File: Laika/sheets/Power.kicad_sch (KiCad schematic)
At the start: 0 parts

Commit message: Created 3.3V Buck Regulator Circuit
Created schematic for a 3.3V buck regulator. All component selection and
calaculation was performed using TI WEBENCH Power designer, of which the
artifacts are stored in 'calc'. Created Netclasses for PWR and USB.
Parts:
- added C1, C5: 10u, Capacitor_SMD:C_0805_2012Metric, symbol Device:C
- added C2, C3: 100n, Capacitor_SMD:C_0805_2012Metric, symbol Device:C
- added C4, C6: 22u, Capacitor_SMD:C_0805_2012Metric, symbol Device:C
- added L1: 4.7u, Inductor_SMD:L_Bourns-SRN8040_8x8.15mm, symbol Device:L
- added R3: 30, Resistor_SMD:R_0603_1608Metric, symbol Device:R
- added R4: 30.9k, Resistor_SMD:R_0603_1608Metric, symbol Device:R
- added R5: 10k, Resistor_SMD:R_0603_1608Metric, symbol Device:R
- added U3: TPS56339DDC, Package_TO_SOT_SMD:SOT-23-6, symbol Regulator_Switching:TPS56339DDC
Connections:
- new net: C3.1, R3.2
- new net: R4.1, R5.2, U3.4 (FB)
- new net: R3.1, U3.6 (BOOT)
- new net: C4.2, C6.1
- new net: C1.2, C5.1
- new net +3V3: C4.1, L1.2, R4.2
- new net BUCK_OUT: C3.2, L1.1, U3.2 (SW)
- new net GND: C2.2, C5.2, C6.2, R5.1, U3.1 (GND)
- new net VDD: C1.1, C2.1, U3.3 (VIN)
- no-connect marks 0 -> 1
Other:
- note added: "3.3V Buck Regulator"
- note added: "Cbst 100.0 nF 35.47 Ohm"
- note added: "Cin 10.0 uF 5.463 mOhm"
- note added: "Cinx 100.0 nF 35.47 mOhm"
- note added: "Cout 22.0 uF 1.603 mOhm"
- note added: "L1 4.7 uH 24.0 mOhm"
- note added: "Power & Battery Management"
- note added: "Rbst 30.0 Ohm 100.0 mW"
- note added: "Rfbb 10.0 kOhm 100.0 mW"
- note added: "Rfbt 30.9 kOhm 100.0 mW"
- note added: "VinMin = 5.0 V VinMax = 12.0 V Vout = 3.3 V Iout = 2.0 A"

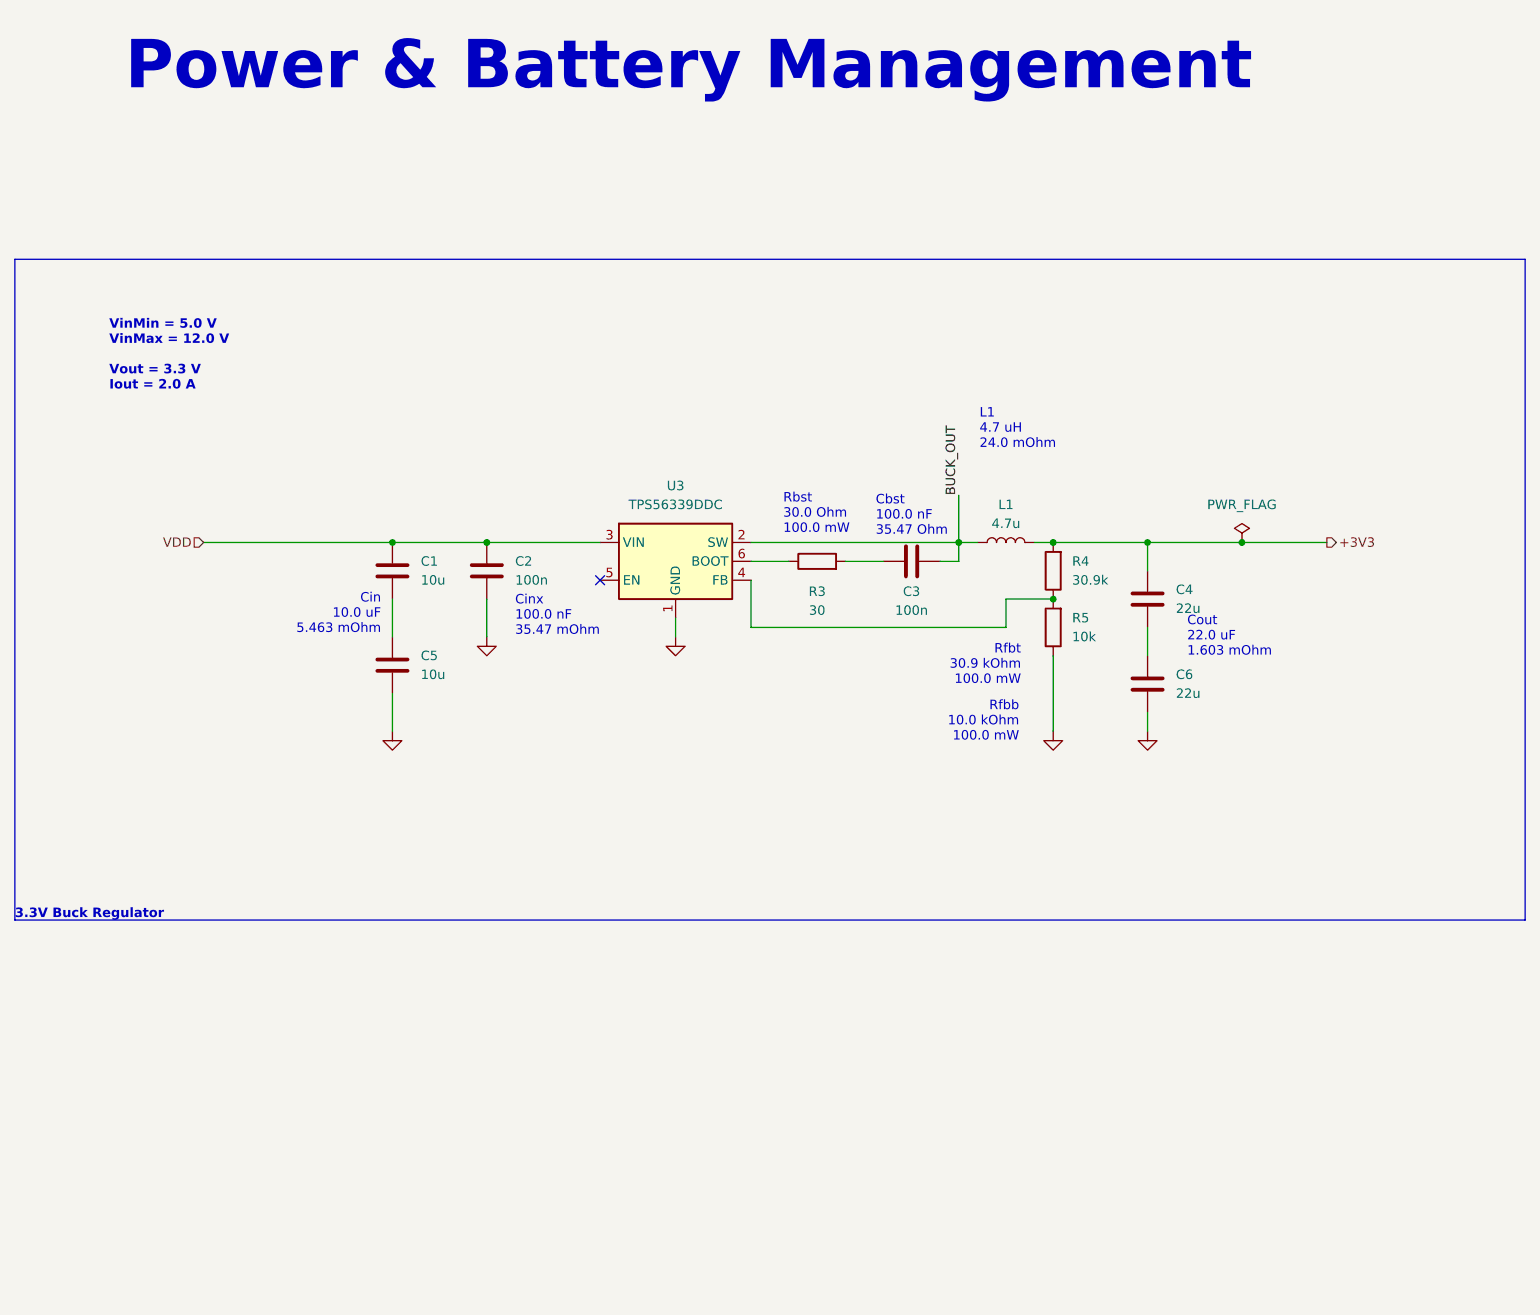
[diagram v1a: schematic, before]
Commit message: Created 1.8V LDO circuit, assigned Mfr Part Numbers to Power IC's
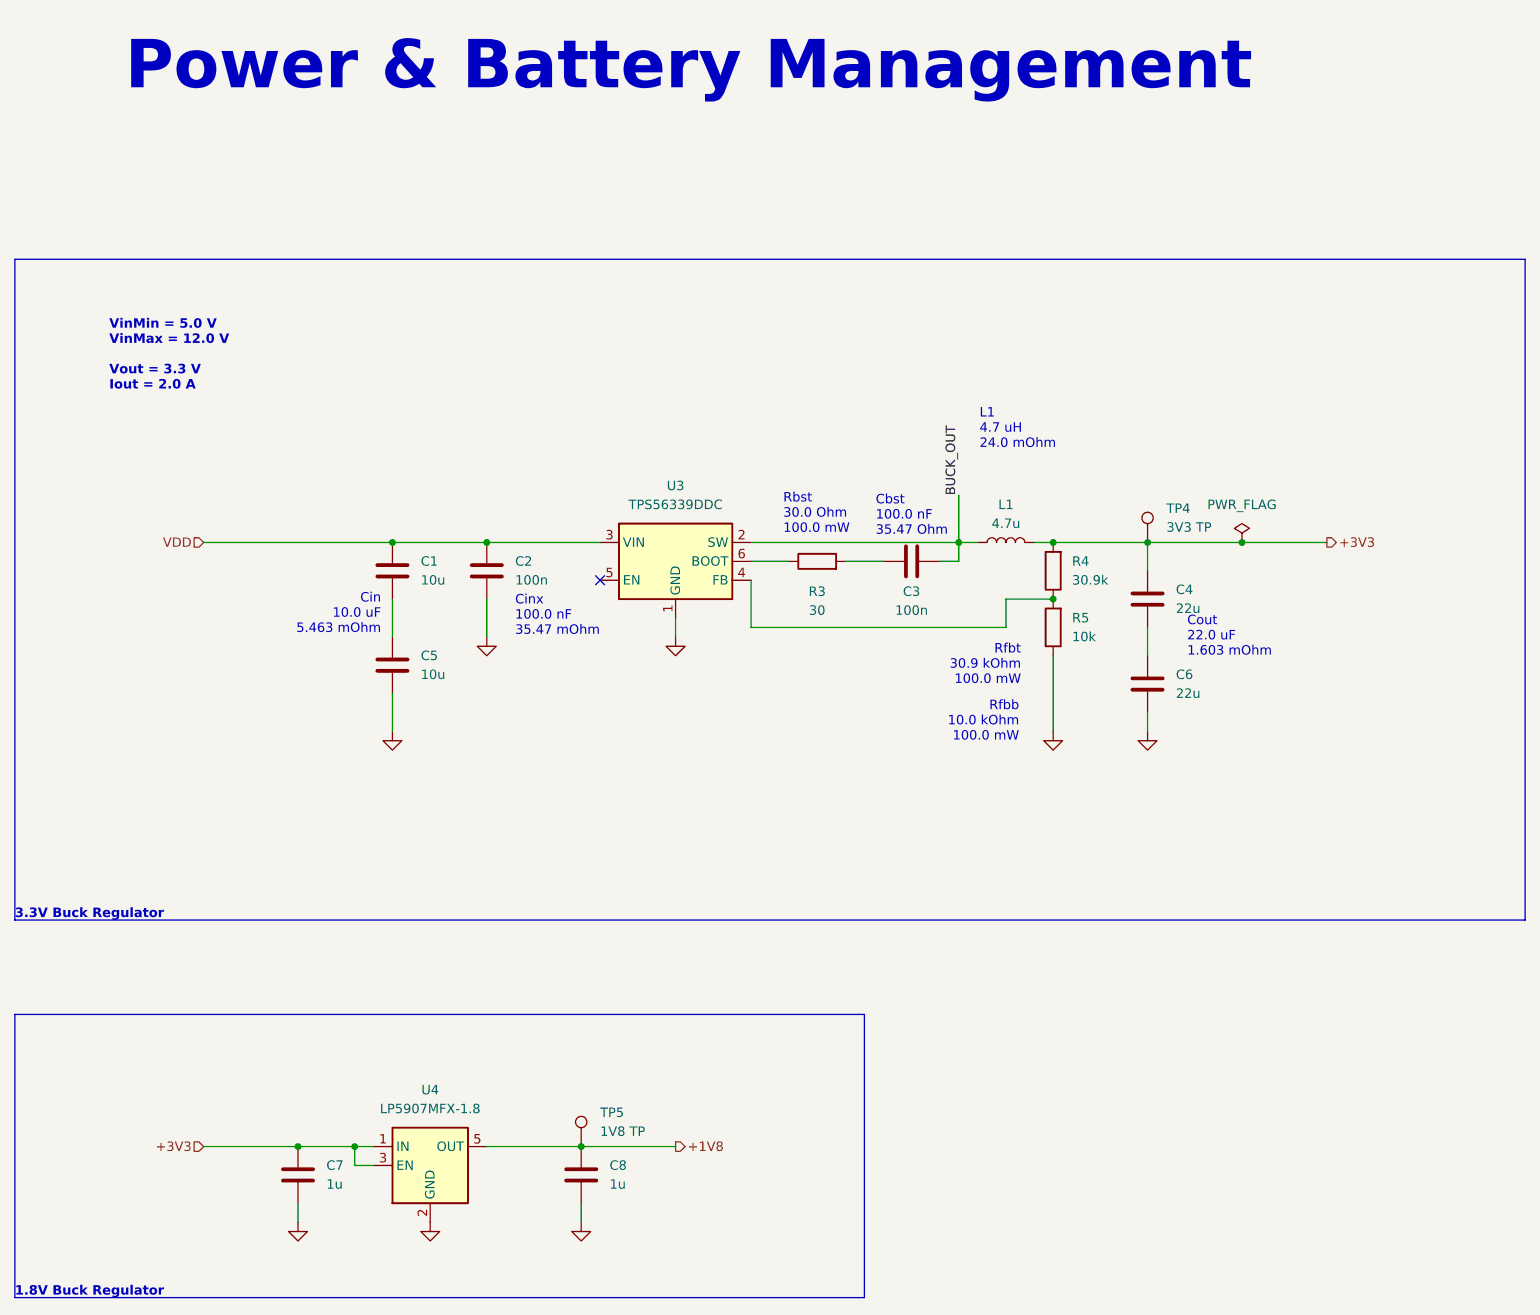
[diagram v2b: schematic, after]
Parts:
- added C7, C8: 1u, symbol Device:C
- added TP4: 3V3 TP, TestPoint:TestPoint_Pad_1.0x1.0mm, symbol Connector:TestPoint
- added TP5: 1V8 TP, TestPoint:TestPoint_Pad_1.0x1.0mm, symbol Connector:TestPoint
- added U4: LP5907MFX-1.8, Package_SON:Texas_X2SON-4_1x1mm_P0.65mm, symbol Regulator_Linear:LP5907MFX-1.8
- U3: Manafacturer (none) -> Texas Instruments; Part Number (none) -> TPS56339DDCR
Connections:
- net +3V3: now also C7.1, TP4.1, U4.1 (IN), U4.3 (EN)
- net GND: now also C7.2, C8.2, U4.2 (GND)
- new net +1V8: C8.1, TP5.1, U4.5 (OUT)
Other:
- note added: "1.8V Buck Regulator"

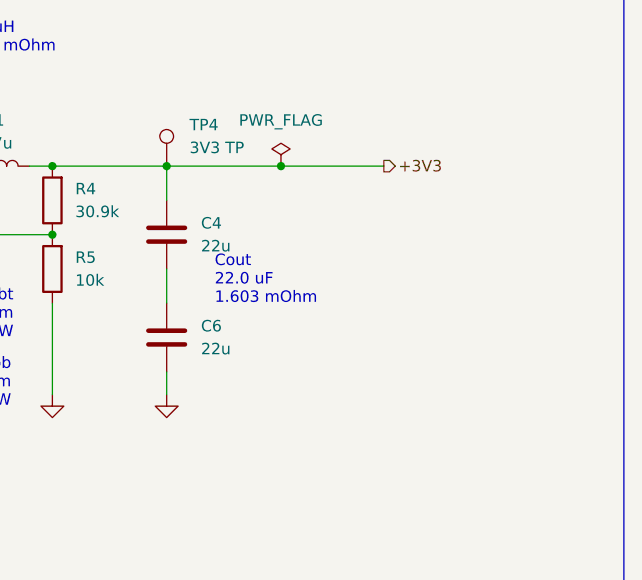
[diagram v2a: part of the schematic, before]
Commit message: Added 3v3 Power LED
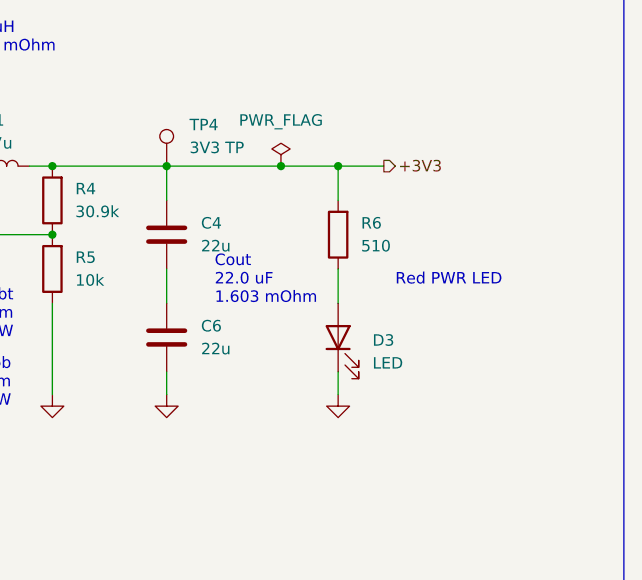
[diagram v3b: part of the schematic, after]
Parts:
- added D3: LED, symbol Device:LED
- added R6: 510, symbol Device:R
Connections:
- net +3V3: now also R6.2
- net GND: now also D3.1 (K)
- new net: D3.2 (A), R6.1
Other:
- note added: "Red PWR LED"

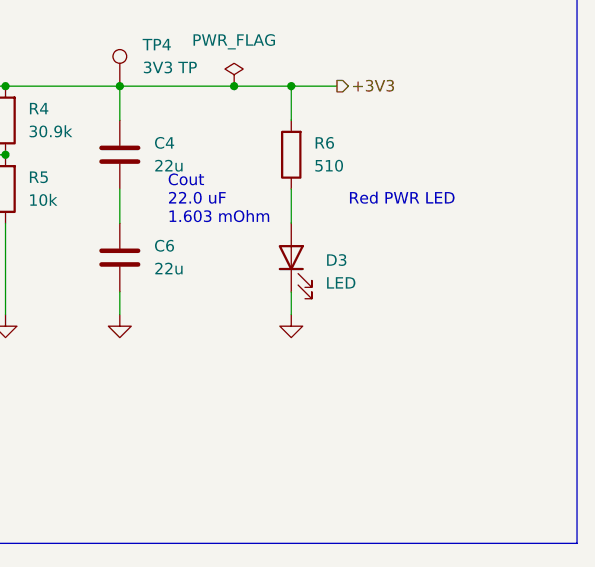
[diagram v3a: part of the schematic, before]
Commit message: Populated BOM with part numbers and footprints
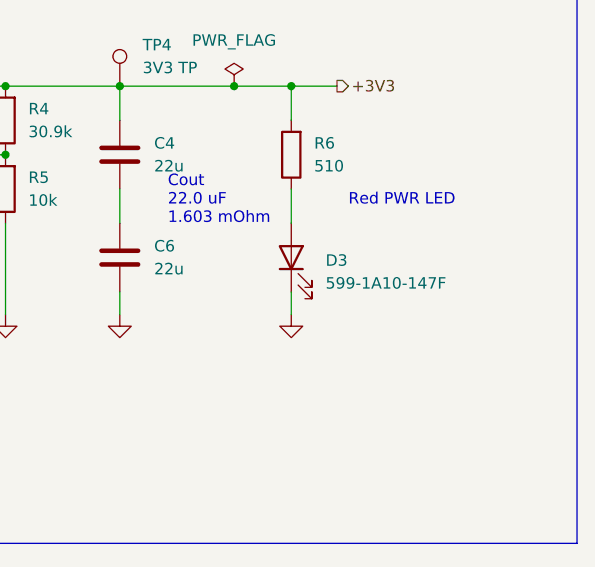
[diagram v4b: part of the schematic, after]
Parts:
- C1, C2, C3, C4, C5, C6, L1, R3, R4, R5, U3, U4: JLC Part Type (none) -> Extended
- C7, C8: footprint (none) -> Capacitor_SMD:C_0402_1005Metric; JLC Part Type (none) -> Basic; Manafacturer (none) -> Samsung Electro-Mechanics; Part Number (none) -> CL05A105KA5NQNC
- D3: value LED -> 599-1A10-147F; footprint (none) -> LED_SMD:LED_0402_1005Metric; Manafacturer (none) -> Dialight; Part Number (none) -> 599-1A10-147F
- R6: footprint (none) -> Resistor_SMD:R_0402_1005Metric_Pad0.72x0.64mm_HandSolder; JLC Part Type (none) -> Basic; Manafacturer (none) -> Royalohm; Part Number (none) -> 0402WGF5100TCE
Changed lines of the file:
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@@
+			)
+		)
+		(property "JLC Part Type" "Extended"
+			(at 106.68 172.72 0)
+			(effects
+				(font
+					(size 1.27 1.27)
+				)
+				(hide yes)
 			)
 		)
@@
 			)
 		)
-		(property "Datasheet" "~"
+		(property "Datasheet" "https://www.mouser.com/datasheet/3/72/1/KEM_C1002_X7R_SMD.pdf"
 			(at 171.45 91.44 0)
 			(effects
@@
 			)
 		)
-		(property "JLC Part Type" ""
+		(property "JLC Part Type" "Extended"
 			(at 171.45 91.44 90)
 			(effects
@@
 			)
 		)
-		(property "JLC Part Type" ""
+		(property "JLC Part Type" "Extended"
 			(at 139.7 91.44 0)
 			(effects
@@
 			)
 		)
-		(property "Datasheet" "~"
+		(property "Datasheet" "https://www.vishay.com/docs/20035/dcrcwe3.pdf"
 			(at 190.5 92.71 0)
 			(effects
@@
 			)
 		)
-		(property "JLC Part Type" ""
+		(property "JLC Part Type" "Extended"
 			(at 190.5 92.71 0)
 			(effects
@@
 			)
 		)
-		(property "Datasheet" "~"
+		(property "Datasheet" "https://www.bourns.com/docs/Product-Datasheets/SRN8040.pdf"
 			(at 184.15 88.9 0)
 			(effects
@@
 			)
 		)
-		(property "JLC Part Type" ""
+		(property "JLC Part Type" "Extended"
 			(at 184.15 88.9 90)
 			(effects
@@
 			)
 		)
-		(property "Datasheet" "~"
+		(property "Datasheet" "https://product.tdk.com/system/files/dam/doc/product/capacitor/ceramic/mlcc/catalog/mlcc_commercial_general_en.pdf"
 			(at 203.2 107.95 0)
 			(effects
@@
 			)
 		)
-		(property "JLC Part Type" ""
+		(property "JLC Part Type" "Extended"
 			(at 203.2 107.95 0)
 			(effects
@@
 			)
 		)
-		(property "Value" "LED"
+		(property "Value" "599-1A10-147F"
 			(at 226.06 110.8074 90)
 			(effects
@@
 			)
 		)
-		(property "Footprint" ""
+		(property "Footprint" "LED_SMD:LED_0402_1005Metric"
 			(at 222.25 107.95 0)
 			(effects
@@
 			)
 		)
-		(property "Datasheet" "~"
+		(property "Datasheet" "https://www.mouser.com/datasheet/3/350/1/C18789.pdf"
 			(at 222.25 107.95 0)
 			(effects
@@
 		(property "Sim.Pins" "1=K 2=A"
 			(at 222.25 107.95 0)
+			(effects
+				(font
+					(size 1.27 1.27)
+				)
+				(hide yes)
+			)
+		)
+		(property "Manafacturer" "Dialight"
+			(at 222.25 107.95 90)
+			(effects
+				(font
+					(size 1.27 1.27)
+				)
+				(hide yes)
+			)
+		)
+		(property "Part Number" "599-1A10-147F "
+			(at 222.25 107.95 90)
 			(effects
 				(font
@@
 			)
 		)
-		(property "Datasheet" "~"
+		(property "Datasheet" "https://www.mouser.com/catalog/specsheets/YAGEO_PYu_RC_Group_51_RoHS_L_12.pdf"
 			(at 190.5 100.33 0)
 			(effects
@@
 			)
 		)
-		(property "JLC Part Type" ""
+		(property "JLC Part Type" "Extended"
 			(at 190.5 100.33 0)
 			(effects
@@
 			)
 		)
-		(property "Footprint" ""
+		(property "Footprint" "Capacitor_SMD:C_0402_1005Metric"
 			(at 89.8652 177.8 0)
 			(effects
@@
 			)
 		)
-		(property "Datasheet" "~"
+		(property "Datasheet" "https://www.samsungsem.com/resources/file/global/support/product_catalog/MLCC.pdf"
 			(at 88.9 173.99 0)
 			(effects
@@
 		)
 		(property "Description" "Unpolarized capacitor"
+			(at 88.9 173.99 0)
+			(effects
+				(font
+					(size 1.27 1.27)
+				)
+				(hide yes)
+			)
+		)
+		(property "JLC Part Type" "Basic"
+			(at 88.9 173.99 0)
+			(effects
+				(font
+					(size 1.27 1.27)
+				)
+				(hide yes)
+			)
+		)
+		(property "Manafacturer" "Samsung Electro-Mechanics"
+			(at 88.9 173.99 0)
+			(effects
+				(font
+					(size 1.27 1.27)
+				)
+				(hide yes)
+			)
+		)
+		(property "Part Number" "CL05A105KA5NQNC"
 			(at 88.9 173.99 0)
 			(effects
@@
 			)
 		)
-		(property "Datasheet" "~"
+		(property "Datasheet" "https://product.tdk.com/system/files/dam/doc/product/capacitor/ceramic/mlcc/catalog/mlcc_commercial_general_en.pdf"
 			(at 203.2 96.52 0)
 			(effects
@@
 			)
 		)
-		(property "JLC Part Type" ""
+		(property "JLC Part Type" "Extended"
 			(at 203.2 96.52 0)
 			(effects
@@
 			)
 		)
-		(property "Datasheet" "~"
+		(property "Datasheet" "https://www.mouser.com/catalog/specsheets/Tayio_Yuden_1102023_MS_mlcc_all_e.pdf"
 			(at 101.6 92.71 0)
 			(effects
@@
 			)
 		)
-		(property "JLC Part Type" ""
+		(property "JLC Part Type" "Extended"
 			(at 101.6 92.71 0)
 			(effects
@@
 			)
 		)
-		(property "Datasheet" "~"
+		(property "Datasheet" "https://www.mouser.com/catalog/specsheets/Tayio_Yuden_1102023_MS_mlcc_all_e.pdf"
 			(at 101.6 105.41 0)
 			(effects
@@
 			)
 		)
-		(property "JLC Part Type" ""
+		(property "JLC Part Type" "Extended"
 			(at 101.6 105.41 0)
 			(effects
@@
 			)
 		)
-		(property "Datasheet" "~"
+		(property "Datasheet" "https://www.mouser.com/catalog/specsheets/YAGEO_PYu_RC_Group_51_RoHS_L_12.pdf"
 			(at 158.75 91.44 0)
 			(effects
@@
 			)
 		)
-		(property "JLC Part Type" ""
+		(property "JLC Part Type" "Extended"
 			(at 158.75 91.44 90)
 			(effects
@@
 			)
 		)
-		(property "Footprint" ""
+		(property "Footprint" "Capacitor_SMD:C_0402_1005Metric"
 			(at 127.9652 177.8 0)
 			(effects
@@
 			)
 		)
-		(property "Datasheet" "~"
+		(property "Datasheet" "https://www.samsungsem.com/resources/file/global/support/product_catalog/MLCC.pdf"
 			(at 127 173.99 0)
 			(effects
@@
 		)
 		(property "Description" "Unpolarized capacitor"
+			(at 127 173.99 0)
+			(effects
+				(font
+					(size 1.27 1.27)
+				)
+				(hide yes)
+			)
+		)
+		(property "JLC Part Type" "Basic"
+			(at 127 173.99 0)
+			(effects
+				(font
+					(size 1.27 1.27)
+				)
+				(hide yes)
+			)
+		)
+		(property "Manafacturer" "Samsung Electro-Mechanics"
+			(at 127 173.99 0)
+			(effects
+				(font
+					(size 1.27 1.27)
+				)
+				(hide yes)
+			)
+		)
+		(property "Part Number" "CL05A105KA5NQNC"
 			(at 127 173.99 0)
 			(effects
@@
 			)
 		)
-		(property "Datasheet" "~"
+		(property "Datasheet" "https://www.mouser.com/datasheet/3/72/1/KEM_C1002_X7R_SMD.pdf"
 			(at 114.3 92.71 0)
 			(effects
@@
 			)
 		)
-		(property "JLC Part Type" ""
+		(property "JLC Part Type" "Extended"
 			(at 114.3 92.71 0)
 			(effects
@@
 			)
 		)
-		(property "Footprint" ""
+		(property "Footprint" "Resistor_SMD:R_0402_1005Metric_Pad0.72x0.64mm_HandSolder"
 			(at 224.028 96.52 90)
 			(effects
@@
 			)
 		)
-		(property "Datasheet" "~"
+		(property "Datasheet" "https://www.mouser.com/datasheet/3/5925/1/1.pdf"
 			(at 222.25 96.52 0)
 			(effects
@@
 			(at 222.25 96.52 0)
 			(effects
+				(font
+					(size 1.27 1.27)
+				)
+				(hide yes)
+			)
+		)
+		(property "JLC Part Type" "Basic"
+			(at 222.25 96.52 0)
+			(effects
+				(font
+					(size 1.27 1.27)
+				)
+				(hide yes)
+			)
+		)
+		(property "Manafacturer" "Royalohm"
+			(at 222.25 96.52 0)
+			(effects
+				(font
+					(size 1.27 1.27)
+				)
+				(hide yes)
+			)
+		)
+		(property "Part Number" "0402WGF5100TCE"
+			(at 222.25 96.52 0)
+			(effects
